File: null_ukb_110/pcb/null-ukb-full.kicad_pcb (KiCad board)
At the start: 2 copper layers, 426.4 x 121.9 mm, 260 parts, among them K001 CHRY_MX, K021 CHRY_MX, K031 CHRY_MX, K041 CHRY_MX, K051 CHRY_MX, K061 CHRY_MX, K071 CHRY_MX, K081 CHRY_MX, K091 CHRY_MX, K0B1 CHRY_MX, K0C1 CHRY_MX, K0D1 CHRY_MX, K0E1 CHRY_MX, K0F1 CHRY_MX, K0G1 CHRY_MX, K0H1 CHRY_MX, K101 CHRY_MX, K111 CHRY_MX, K121 CHRY_MX, K131 CHRY_MX, K141 CHRY_MX, K151 CHRY_MX, K161 CHRY_MX, K171 CHRY_MX, K181 CHRY_MX, K191 CHRY_MX, K1A1 CHRY_MX, K1B1 CHRY_MX, K1C1 CHRY_MX, K1D1 CHRY_MX, K1E1 CHRY_MX, K1E2 CHRY_MX, K1F1 CHRY_MX, K1G1 CHRY_MX, K1H1 CHRY_MX, K1I1 CHRY_MX, K1J1 CHRY_MX, K1K1 CHRY_MX, K1L1 CHRY_MX, K201 CHRY_MX, K211 CHRY_MX, K221 CHRY_MX, K231 CHRY_MX, K241 CHRY_MX, K251 CHRY_MX, K261 CHRY_MX, K271 CHRY_MX, K281 CHRY_MX, K291 CHRY_MX, K2A1 CHRY_MX, K2B1 CHRY_MX, K2C1 CHRY_MX, K2F1 CHRY_MX, K2G1 CHRY_MX, K2H1 CHRY_MX, K2I1 CHRY_MX, K2J1 CHRY_MX, K2K1 CHRY_MX, K301 CHRY_MX, K311 CHRY_MX, K321 CHRY_MX, K331 CHRY_MX, K341 CHRY_MX, K351 CHRY_MX, K361 CHRY_MX, K371 CHRY_MX, K381 CHRY_MX, K391 CHRY_MX, K3A1 CHRY_MX, K3B1 CHRY_MX, K3C1 CHRY_MX, K3C2 CHRY_MX, K3E1 CHRY_MX, K3E2 CHRY_MX, K3I1 CHRY_MX, K3J1 CHRY_MX, K3K1 CHRY_MX, K3L1 CHRY_MX, K401 CHRY_MX, K402 CHRY_MX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

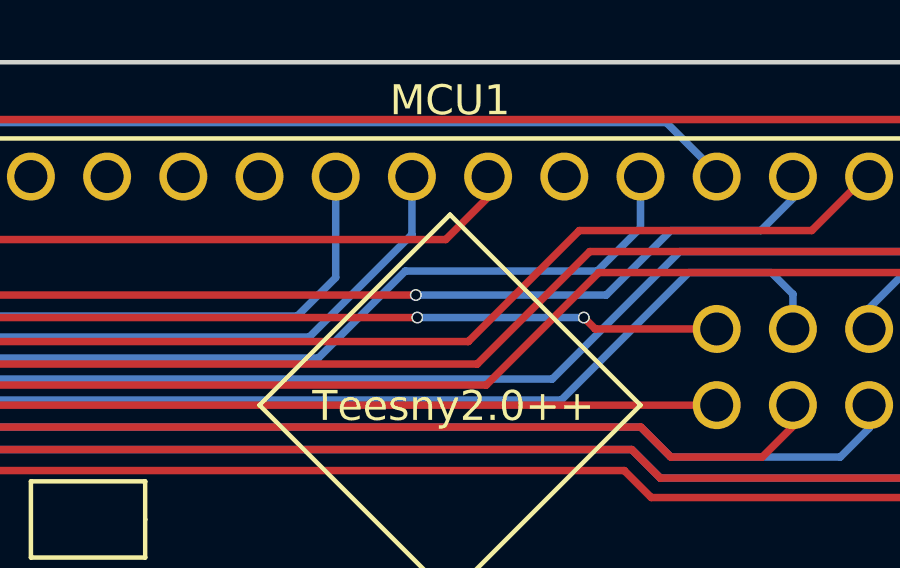
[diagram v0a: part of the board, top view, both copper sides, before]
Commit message: Fixed solder mask over LED pads on back side of board.
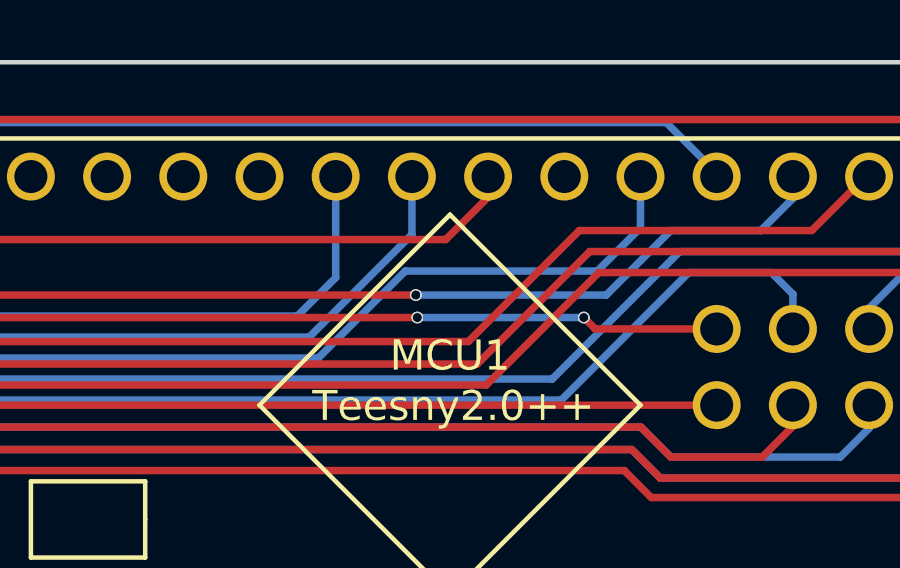
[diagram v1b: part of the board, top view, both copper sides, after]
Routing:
- net Net-(L5D1-Pad2): track 0.00 -> 141.3 mm, vias 0 -> 2
- net Net-(L5A1-Pad2): track 104.1 -> 0.00 mm, vias 1 -> 0
- net /LED_06: track 133.0 -> 95.8 mm, vias 1 -> 0
